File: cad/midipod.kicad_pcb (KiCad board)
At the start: 2 copper layers, 50.8 x 51.4 mm, 22 parts, among them IC1 ATMEGA8U2, M3 1pin, P1 ISP, P2 USB, P3 INV1, P4 SW1, Y1 Crystal

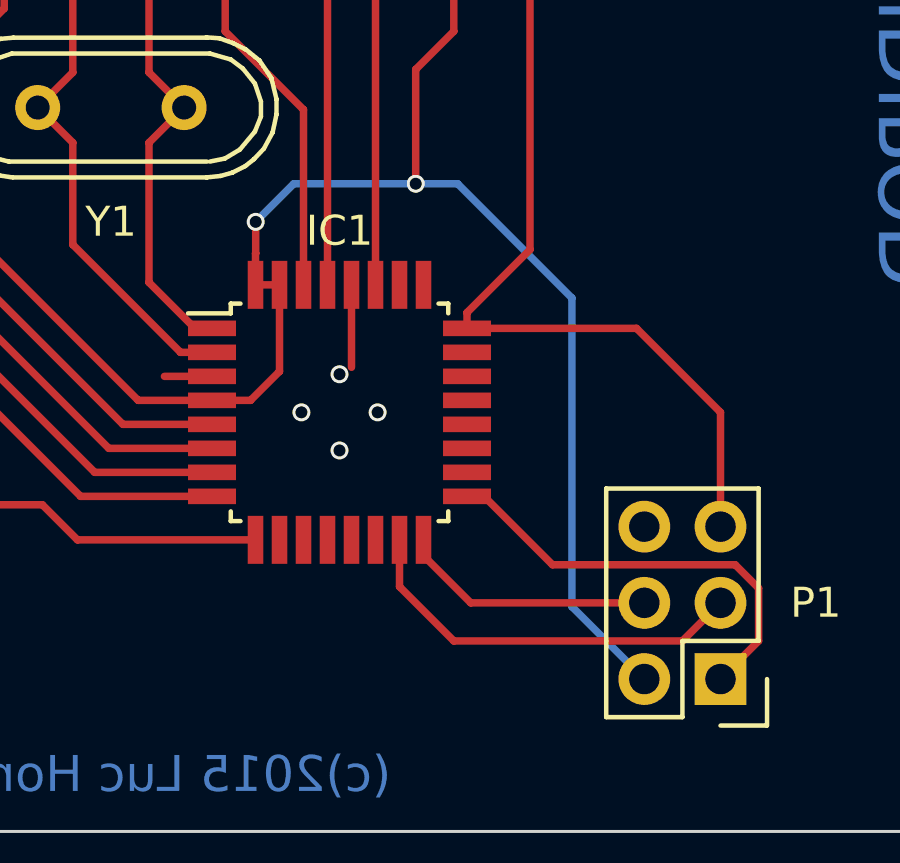
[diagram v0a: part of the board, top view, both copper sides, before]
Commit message: Update to KiCad 6
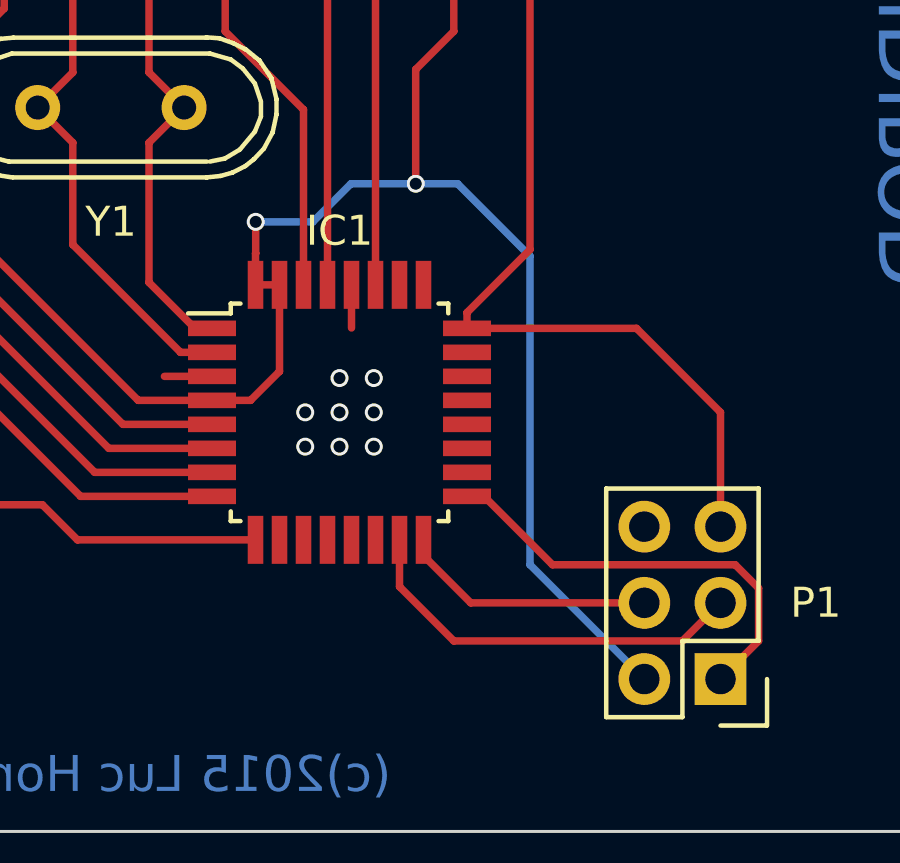
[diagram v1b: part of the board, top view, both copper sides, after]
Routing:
- net GND: track 4.33 -> 3.02 mm, vias 4 -> 8
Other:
- net class Default removed

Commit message: UPdate to KiCad 8
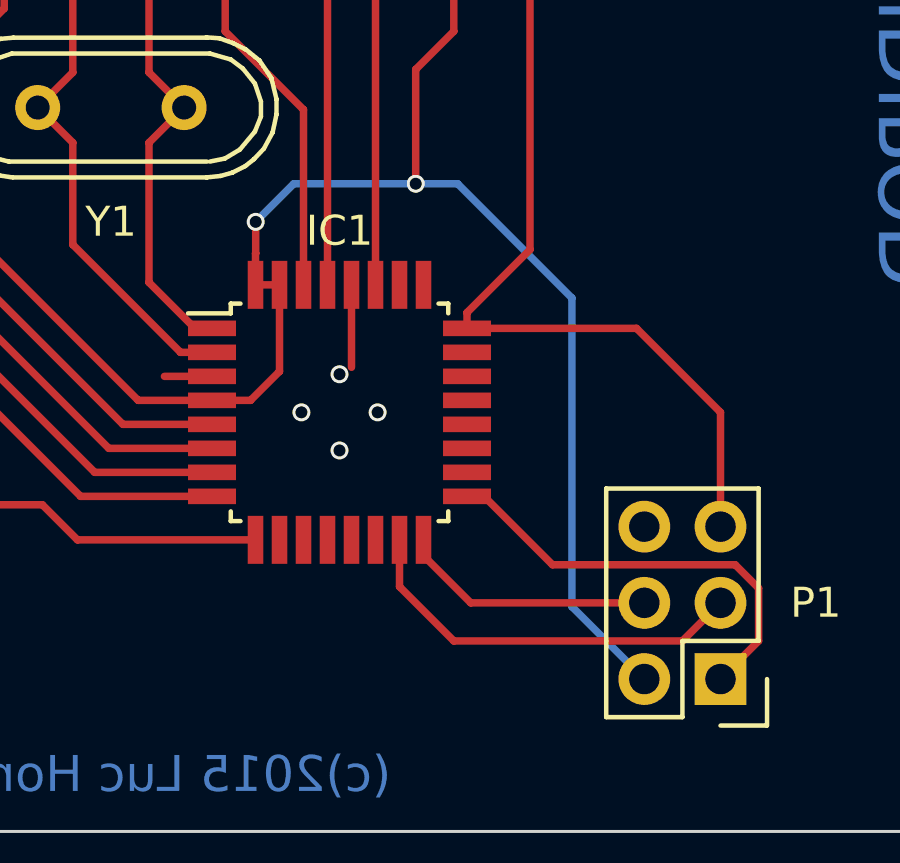
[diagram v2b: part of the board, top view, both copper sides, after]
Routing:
- net GND: track 3.02 -> 4.33 mm, vias 8 -> 4

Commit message: Update to KiCad 9
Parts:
- removed M3 (x2): 1pin, Connect:1pin
- D1, D2: footprint LEDs:LED-3MM -> LED_THT:LED_D3.0mm_Horizontal_O1.27mm_Z2.0mm_Clear
- moved C1 7.62 mm to (153.4, 91.1)
- moved R5 2.54 mm to (158.5, 91.1)
- moved C6 2.54 mm to (161.0, 91.1)
- moved R6 2.54 mm to (156.0, 91.1)
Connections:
- IC1 pad 10: (no net) -> unconnected-(IC1-(INT5/AIN3)PD4-Pad10)
- IC1 pad 11: (no net) -> unconnected-(IC1-(XCK/AIN4/PCINT12)PD5-Pad11)
- IC1 pad 12: (no net) -> unconnected-(IC1-(~{RTS}/AIN5/INT6)PD6-Pad12)
- IC1 pad 13: (no net) -> unconnected-(IC1-(~{CTS}/~{HWB}/AIN6/T0/INT7)PD7-Pad13)
- IC1 pad 14: (no net) -> unconnected-(IC1-(~{SS}/PCINT0)PB0-Pad14)
- IC1 pad 18: (no net) -> unconnected-(IC1-(T1/PCINT4)PB4-Pad18)
- IC1 pad 19: (no net) -> unconnected-(IC1-(PCINT5)PB5-Pad19)
- IC1 pad 20: (no net) -> unconnected-(IC1-(PCINT6)PB6-Pad20)
- IC1 pad 21: (no net) -> unconnected-(IC1-(PCINT7/OC.0A/OC.1C)PB7-Pad21)
- IC1 pad 22: (no net) -> unconnected-(IC1-(INT4/ICP1/CLK0)PC7-Pad22)
- IC1 pad 23: (no net) -> unconnected-(IC1-(OC.1A/PCINT8)PC6-Pad23)
- IC1 pad 25: (no net) -> unconnected-(IC1-(PCINT9/OC.1B)PC5-Pad25)
- IC1 pad 26: (no net) -> unconnected-(IC1-(PCINT10)PC4-Pad26)
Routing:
- net +5V: track 95.6 -> 106.6 mm, vias 2 -> 1
- net Net-(IC1-UCAP): track 12.8 -> 14.1 mm
- net Net-(P2-P2): track 7.47 -> 8.53 mm
- net /DATA-: track 13.9 -> 12.8 mm
- net GND: vias 4 -> 17
